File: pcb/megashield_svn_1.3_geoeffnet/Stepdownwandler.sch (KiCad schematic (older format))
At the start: 15 parts, among them U1 DC 10V, U6 DC 3,3V, U7 DC 5V

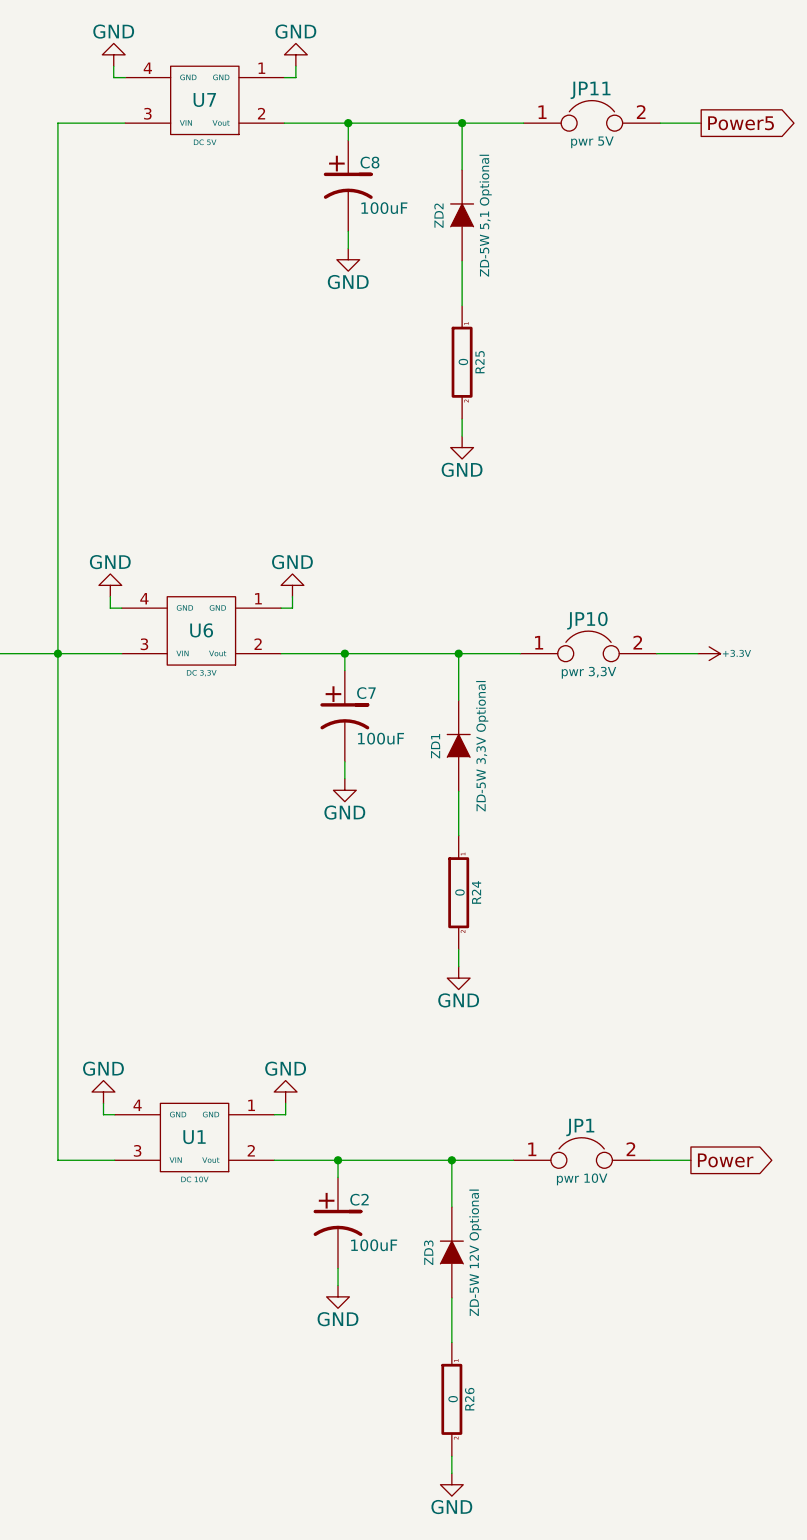
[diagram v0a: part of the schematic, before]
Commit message: Platine V1.3 - 1 Schaltplanentwurf
nur Schaltplan gezeichnet nichts an der Platine
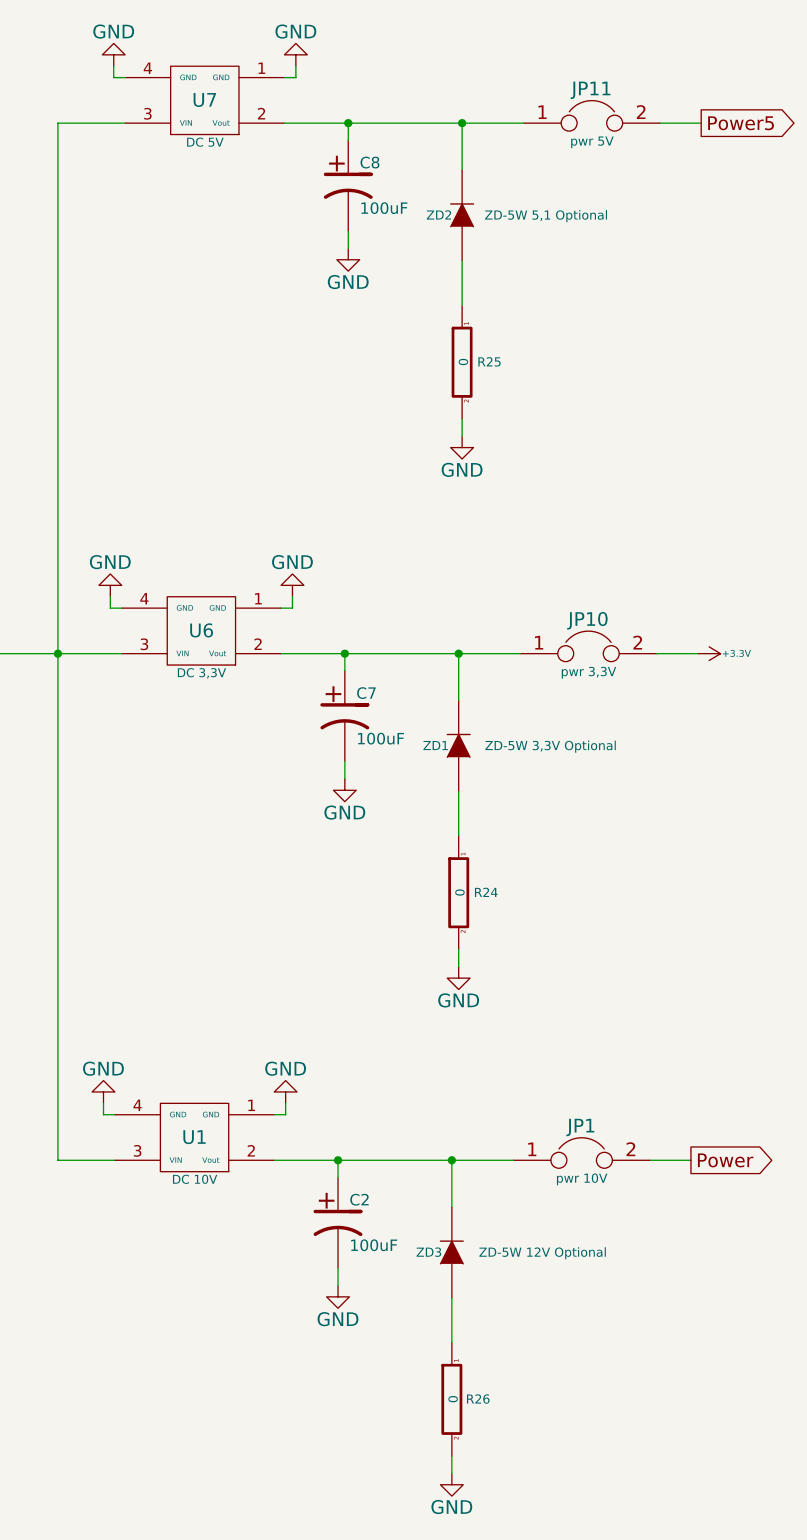
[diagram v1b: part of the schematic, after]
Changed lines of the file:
@@
 $Descr A4 11693 8268
 encoding utf-8
-Sheet 17 17
+Sheet 15 17
 Title ""
 Date ""
@@
 P 4055 1115
 F 0 "U7" H 4055 1115 60  0000 C CNN
-F 1 "DC  5V" H 4055 930 24  0000 C CNN
+F 1 "DC  5V" H 4055 930 39  0000 C CNN
 F 2 "ACS712:DC_DC_DSN2596_mit_Bohrloch_doppelte_Lochreihe" H 4055 1115 60  0001 C CNN
 F 3 "" H 4055 1115 60  0000 C CNN
@@
 U 1 1 553E5DC0
 P 5185 1620
-F 0 "ZD2" H 5185 1720 40  0000 C CNN
-F 1 "ZD-5W 5,1 Optional" H 5185 1520 40  0000 C CNN
+F 0 "ZD2" V 5185 1720 40  0000 C CNN
+F 1 "ZD-5W 5,1 Optional" V 5185 1250 40  0000 C CNN
 F 2 "ACS712:Diode_ligend_RM10" H 5185 1620 60  0001 C CNN
 F 3 "" H 5185 1620 60  0000 C CNN
@@
 U 1 1 553E6E97
 P 5185 2265
-F 0 "R25" V 5265 2265 40  0000 C CNN
+F 0 "R25" H 5305 2265 40  0000 C CNN
 F 1 "0" V 5192 2266 40  0000 C CNN
 F 2 "ACS712:Resistor_Horizontal_RM15mm" V 5115 2265 30  0001 C CNN
@@
 P 4040 3445
 F 0 "U6" H 4040 3445 60  0000 C CNN
-F 1 "DC  3,3V" H 4040 3260 24  0000 C CNN
+F 1 "DC  3,3V" H 4040 3260 39  0000 C CNN
 F 2 "ACS712:DC_DC_DSN2596_mit_Bohrloch_doppelte_Lochreihe" H 4040 3445 60  0001 C CNN
 F 3 "" H 4040 3445 60  0000 C CNN
@@
 U 1 1 553E7CFF
 P 5170 3950
-F 0 "ZD1" H 5170 4050 40  0000 C CNN
-F 1 "ZD-5W 3,3V Optional" H 5170 3850 40  0000 C CNN
+F 0 "ZD1" V 5170 4050 40  0000 C CNN
+F 1 "ZD-5W 3,3V Optional" V 5170 3545 40  0000 C CNN
 F 2 "ACS712:Diode_ligend_RM10" H 5170 3950 60  0001 C CNN
 F 3 "" H 5170 3950 60  0000 C CNN
@@
 U 1 1 553E7D11
 P 5170 4595
-F 0 "R24" V 5250 4595 40  0000 C CNN
+F 0 "R24" H 5290 4595 40  0000 C CNN
 F 1 "0" V 5177 4596 40  0000 C CNN
 F 2 "ACS712:Resistor_Horizontal_RM15mm" V 5100 4595 30  0001 C CNN
@@
 P 4010 5670
 F 0 "U1" H 4010 5670 60  0000 C CNN
-F 1 "DC 10V" H 4010 5485 24  0000 C CNN
+F 1 "DC 10V" H 4010 5485 39  0000 C CNN
 F 2 "ACS712:DC_DC_DSN2596_mit_Bohrloch_doppelte_Lochreihe" H 4010 5670 60  0001 C CNN
 F 3 "" H 4010 5670 60  0000 C CNN
@@
 U 1 1 553E9139
 P 5140 6175
-F 0 "ZD3" H 5140 6275 40  0000 C CNN
-F 1 "ZD-5W 12V Optional" H 5140 6075 40  0000 C CNN
+F 0 "ZD3" V 5140 6275 40  0000 C CNN
+F 1 "ZD-5W 12V Optional" V 5140 5775 40  0000 C CNN
 F 2 "ACS712:Diode_ligend_RM10" H 5140 6175 60  0001 C CNN
 F 3 "" H 5140 6175 60  0000 C CNN
@@
 U 1 1 553E914B
 P 5140 6820
-F 0 "R26" V 5220 6820 40  0000 C CNN
+F 0 "R26" H 5255 6820 40  0000 C CNN
 F 1 "0" V 5147 6821 40  0000 C CNN
 F 2 "ACS712:Resistor_Horizontal_RM15mm" V 5070 6820 30  0001 C CNN

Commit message: Platine V1.3
Grundgerüst fertig
LED Schaltung muss noch geändert werden und RC Änderung
Bauteil Bezeichnungen, Schaltplan; Abmessungen und Duoadapter müssen
überprüft werden.
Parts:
- JP1, JP10, JP11: footprint Pin_Headers:Pin_Header_Straight_1x02 -> ACS712:Pin_Header_Straight_1x02
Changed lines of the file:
@@
 EESchema Schematic File Version 2
-LIBS:Lötpad_2,5mm
+LIBS:Wlan_ESP8266
 LIBS:power
-LIBS:Bluetooth_ZS_HC_05
-LIBS:Bluetooth_CZ_HC_05
-LIBS:ds1307
-LIBS:Wlan_ESP8266
-LIBS:transistor-fet
-LIBS:transistor-fet+irf7201
-LIBS:transistors
-LIBS:w_transistor
-LIBS:diode
-LIBS:diode-1
-LIBS:led
 LIBS:ardumower mega shield svn-cache
 EELAYER 25 0
@@
 $Descr A4 11693 8268
 encoding utf-8
-Sheet 15 17
-Title ""
+Sheet 19 24
+Title "Ardumower Shield - Stepdownwandler"
 Date ""
-Rev ""
-Comp "von UweZ"
+Rev "V1.3"
+Comp "Layout & Plan von UweZ"
 Comment1 ""
 Comment2 ""
@@
 $EndComp
 $Comp
-L GND #PWR0147
+L GND #PWR0146
 U 1 1 553E58DC
 P 4455 965
-F 0 "#PWR0147" H 4455 715 60  0001 C CNN
+F 0 "#PWR0146" H 4455 715 60  0001 C CNN
 F 1 "GND" H 4455 815 60  0000 C CNN
 F 2 "" H 4455 965 60  0000 C CNN
@@
 $EndComp
 $Comp
-L GND #PWR0148
+L GND #PWR0147
 U 1 1 553E58FB
 P 3655 965
-F 0 "#PWR0148" H 3655 715 60  0001 C CNN
+F 0 "#PWR0147" H 3655 715 60  0001 C CNN
 F 1 "GND" H 3655 815 60  0000 C CNN
 F 2 "" H 3655 965 60  0000 C CNN
@@
 $EndComp
 $Comp
-L GND #PWR0149
+L GND #PWR0148
 U 1 1 553E7071
 P 5185 2590
-F 0 "#PWR0149" H 5185 2340 60  0001 C CNN
+F 0 "#PWR0148" H 5185 2340 60  0001 C CNN
 F 1 "GND" H 5185 2440 60  0000 C CNN
 F 2 "" H 5185 2590 60  0000 C CNN
@@
 F 0 "JP11" H 5755 1365 60  0000 C CNN
 F 1 "pwr 5V" H 5755 1135 40  0000 C CNN
-F 2 "Pin_Headers:Pin_Header_Straight_1x02" H 5755 1215 60  0001 C CNN
+F 2 "ACS712:Pin_Header_Straight_1x02" H 5755 1215 60  0001 C CNN
 F 3 "" H 5755 1215 60  0000 C CNN
 	1    5755 1215
@@
 	5185 1820 5185 2015
 $Comp
-L GND #PWR0150
+L GND #PWR0149
 U 1 1 553E76F0
 P 4685 1765
-F 0 "#PWR0150" H 4685 1515 60  0001 C CNN
+F 0 "#PWR0149" H 4685 1515 60  0001 C CNN
 F 1 "GND" H 4685 1615 60  0000 C CNN
 F 2 "" H 4685 1765 60  0000 C CNN
@@
 $EndComp
 $Comp
-L GND #PWR0151
+L GND #PWR0150
 U 1 1 553E7CEE
 P 4440 3295
-F 0 "#PWR0151" H 4440 3045 60  0001 C CNN
+F 0 "#PWR0150" H 4440 3045 60  0001 C CNN
 F 1 "GND" H 4440 3145 60  0000 C CNN
 F 2 "" H 4440 3295 60  0000 C CNN
@@
 $EndComp
 $Comp
-L GND #PWR0152
+L GND #PWR0151
 U 1 1 553E7CF4
 P 3640 3295
-F 0 "#PWR0152" H 3640 3045 60  0001 C CNN
+F 0 "#PWR0151" H 3640 3045 60  0001 C CNN
 F 1 "GND" H 3640 3145 60  0000 C CNN
 F 2 "" H 3640 3295 60  0000 C CNN
@@
 $EndComp
 $Comp
-L GND #PWR0153
+L GND #PWR0152
 U 1 1 553E7D17
 P 5170 4920
-F 0 "#PWR0153" H 5170 4670 60  0001 C CNN
+F 0 "#PWR0152" H 5170 4670 60  0001 C CNN
 F 1 "GND" H 5170 4770 60  0000 C CNN
 F 2 "" H 5170 4920 60  0000 C CNN
@@
 F 0 "JP10" H 5740 3695 60  0000 C CNN
 F 1 "pwr 3,3V" H 5740 3465 40  0000 C CNN
-F 2 "Pin_Headers:Pin_Header_Straight_1x02" H 5740 3545 60  0001 C CNN
+F 2 "ACS712:Pin_Header_Straight_1x02" H 5740 3545 60  0001 C CNN
 F 3 "" H 5740 3545 60  0000 C CNN
 F 4 "Value" H 5740 3545 60  0001 C CNN "Bestellnummer"
@@
 	5170 4150 5170 4345
 $Comp
-L GND #PWR0154
+L GND #PWR0153
 U 1 1 553E7D26
 P 4670 4095
-F 0 "#PWR0154" H 4670 3845 60  0001 C CNN
+F 0 "#PWR0153" H 4670 3845 60  0001 C CNN
 F 1 "GND" H 4670 3945 60  0000 C CNN
 F 2 "" H 4670 4095 60  0000 C CNN
@@
 	6040 3545 6220 3545
 $Comp
-L +3.3V #PWR0155
+L +3.3V #PWR0154
 U 1 1 553E8B9E
 P 6220 3545
-F 0 "#PWR0155" H 6220 3505 30  0001 C CNN
+F 0 "#PWR0154" H 6220 3505 30  0001 C CNN
 F 1 "+3.3V" V 6220 3715 30  0000 C CNN
 F 2 "" H 6220 3545 60  0000 C CNN
@@
 $EndComp
 $Comp
-L GND #PWR0156
+L GND #PWR0155
 U 1 1 553E9128
 P 4410 5520
-F 0 "#PWR0156" H 4410 5270 60  0001 C CNN
+F 0 "#PWR0155" H 4410 5270 60  0001 C CNN
 F 1 "GND" H 4410 5370 60  0000 C CNN
 F 2 "" H 4410 5520 60  0000 C CNN
@@
 $EndComp
 $Comp
-L GND #PWR0157
+L GND #PWR0156
 U 1 1 553E912E
 P 3610 5520
-F 0 "#PWR0157" H 3610 5270 60  0001 C CNN
+F 0 "#PWR0156" H 3610 5270 60  0001 C CNN
 F 1 "GND" H 3610 5370 60  0000 C CNN
 F 2 "" H 3610 5520 60  0000 C CNN
@@
 $EndComp
 $Comp
-L GND #PWR0158
+L GND #PWR0157
 U 1 1 553E9151
 P 5140 7145
-F 0 "#PWR0158" H 5140 6895 60  0001 C CNN
+F 0 "#PWR0157" H 5140 6895 60  0001 C CNN
 F 1 "GND" H 5140 6995 60  0000 C CNN
 F 2 "" H 5140 7145 60  0000 C CNN
@@
 F 0 "JP1" H 5710 5920 60  0000 C CNN
 F 1 "pwr 10V" H 5710 5690 40  0000 C CNN
-F 2 "Pin_Headers:Pin_Header_Straight_1x02" H 5710 5770 60  0001 C CNN
+F 2 "ACS712:Pin_Header_Straight_1x02" H 5710 5770 60  0001 C CNN
 F 3 "" H 5710 5770 60  0000 C CNN
 F 4 "Value" H 5710 5770 60  0001 C CNN "Bestellnummer"
@@
 	5140 6375 5140 6570
 $Comp
-L GND #PWR0159
+L GND #PWR0158
 U 1 1 553E9161
 P 4640 6320
-F 0 "#PWR0159" H 4640 6070 60  0001 C CNN
+F 0 "#PWR0158" H 4640 6070 60  0001 C CNN
 F 1 "GND" H 4640 6170 60  0000 C CNN
 F 2 "" H 4640 6320 60  0000 C CNN

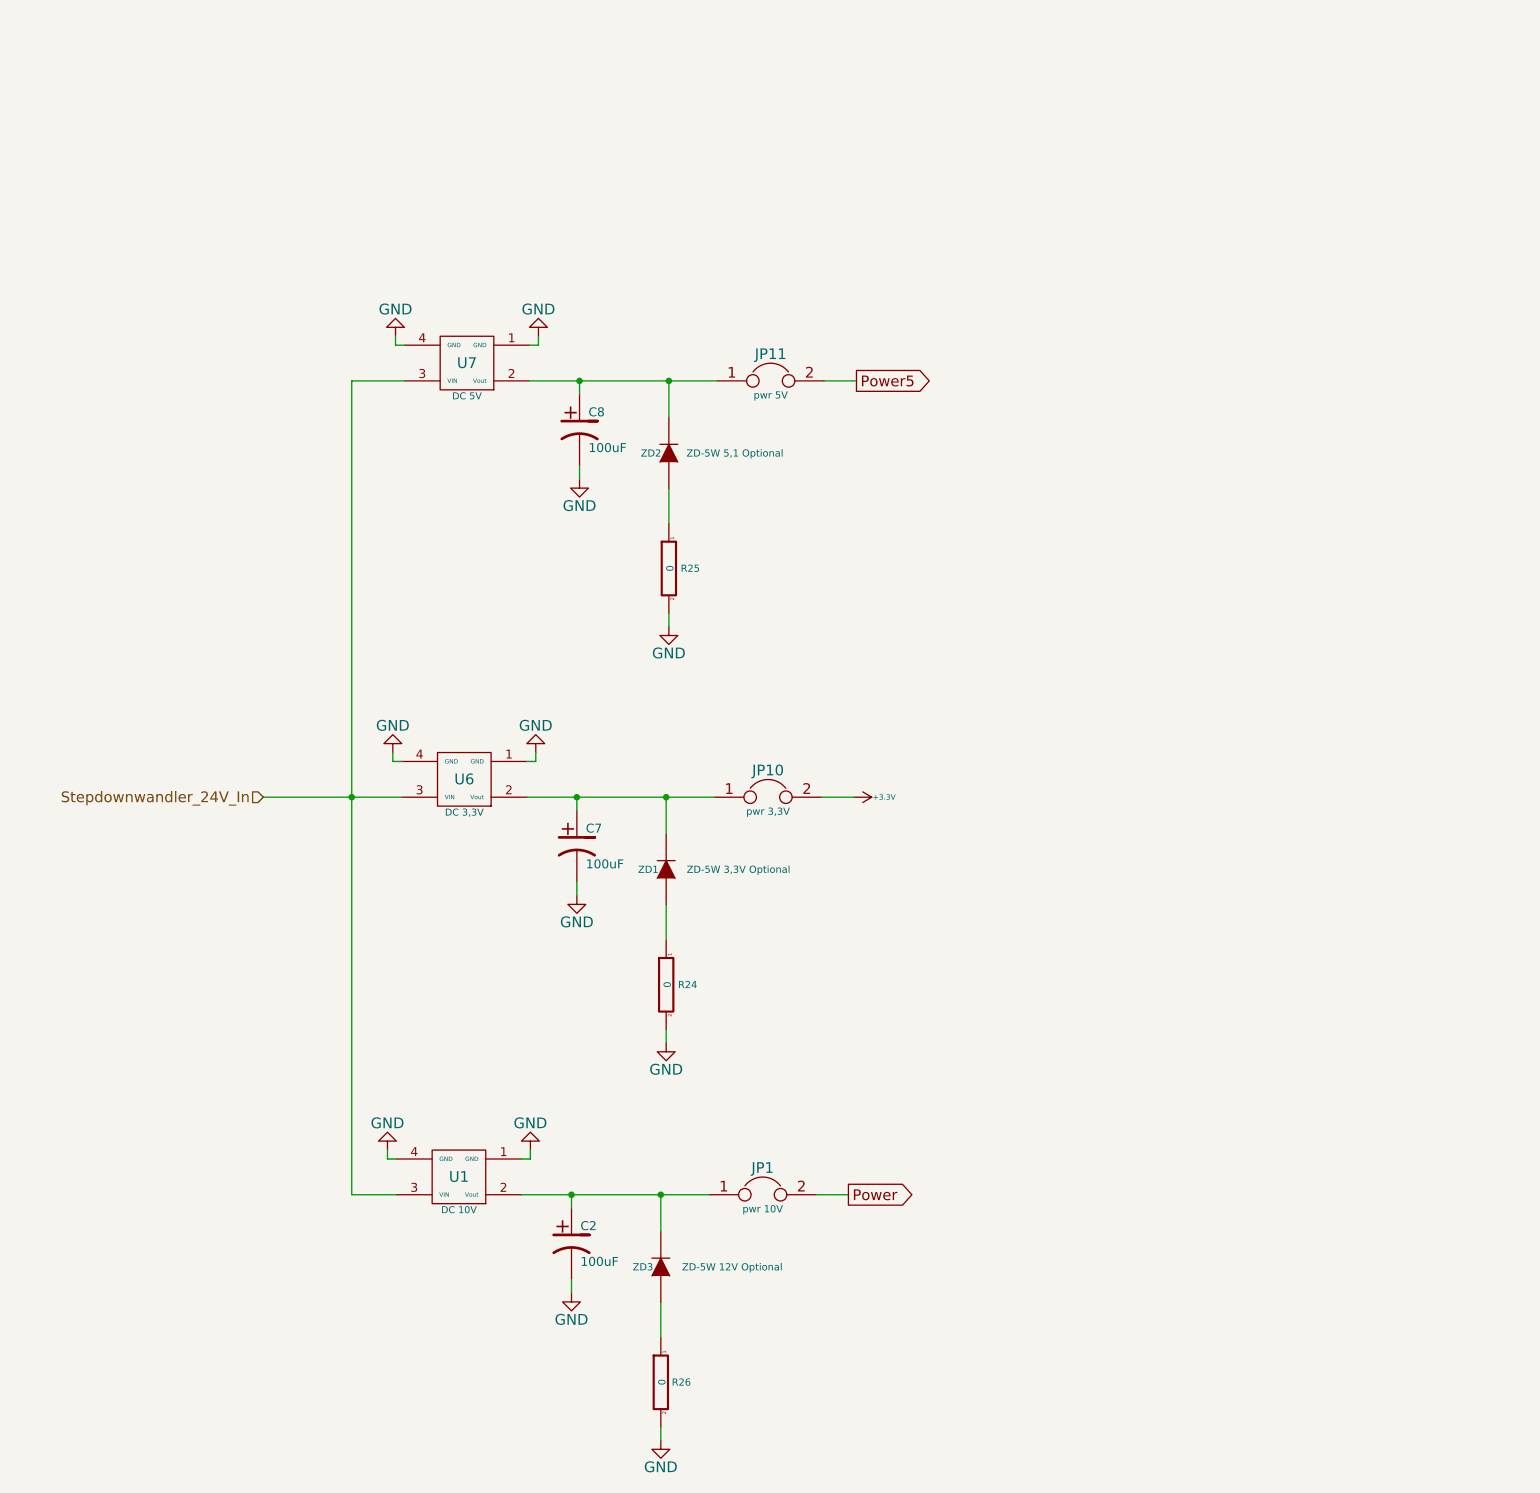
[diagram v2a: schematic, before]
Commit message: Platine V1.3
Sicherung vor den Veränderung und Erweiterungen von Jürgen um dem
entfernen von den Duo Adapter kontakten
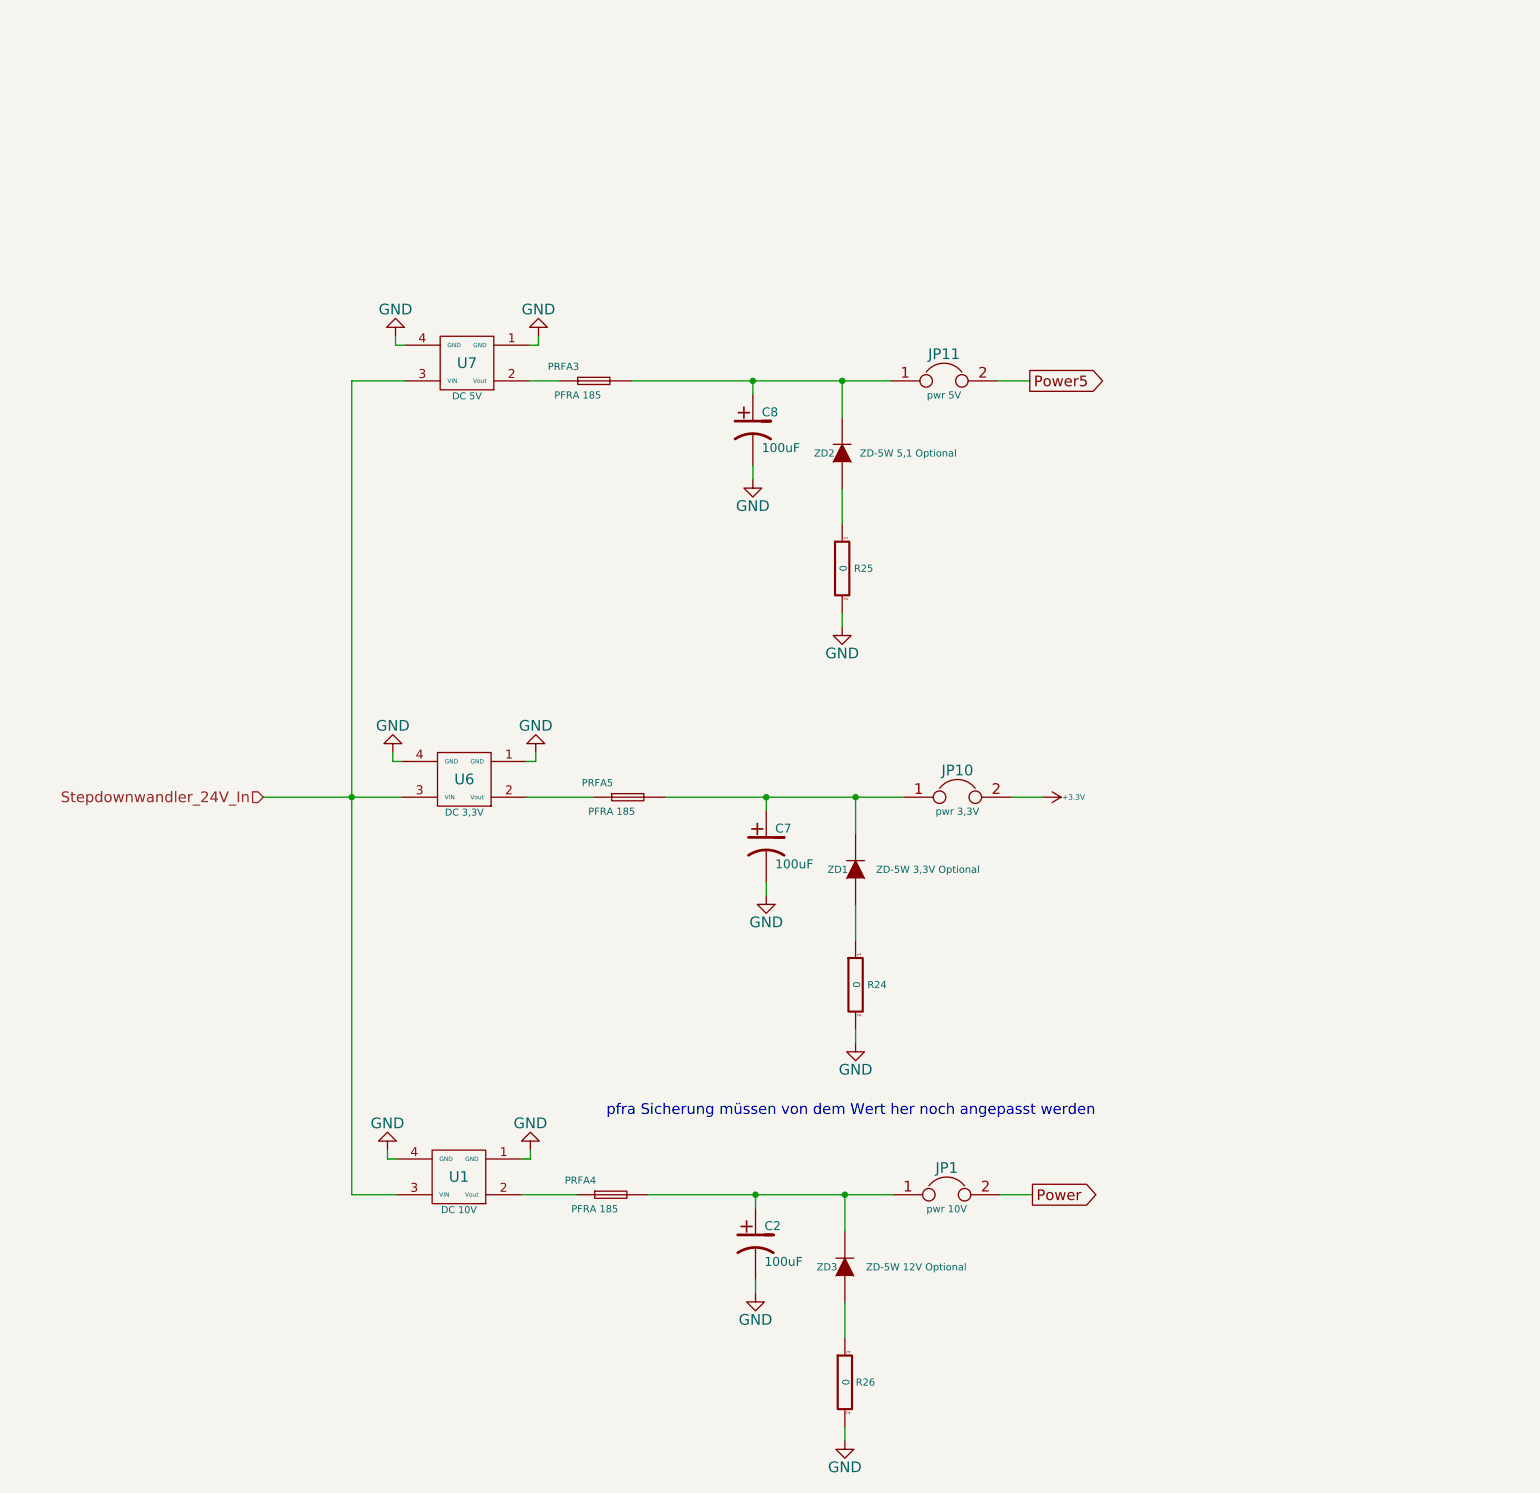
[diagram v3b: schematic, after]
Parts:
- added PRFA3, PRFA4, PRFA5: PFRA 185, ACS712:PRFA_500_stehend, symbol F_10A
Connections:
- net at C8.1, JP11.1, ZD2.2 (K): now also PRFA3.1; no longer U7.2 (Vout)
- net at C7.1, JP10.1, ZD1.2 (K): now also PRFA5.1; no longer U6.2 (Vout)
- net at C2.1, JP1.1, ZD3.2 (K): now also PRFA4.1; no longer U1.2 (Vout)
- new net: PRFA3.2, U7.2 (Vout)
- new net: PRFA5.2, U6.2 (Vout)
- new net: PRFA4.2, U1.2 (Vout)
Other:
- note added: "pfra Sicherung müssen von dem Wert her noch angepasst werden"
- moved on the sheet: C2, C7, C8, JP1, JP10, JP11, R24, R25, R26, ZD1, ZD2, ZD3
